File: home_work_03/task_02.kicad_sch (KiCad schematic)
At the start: 10 parts

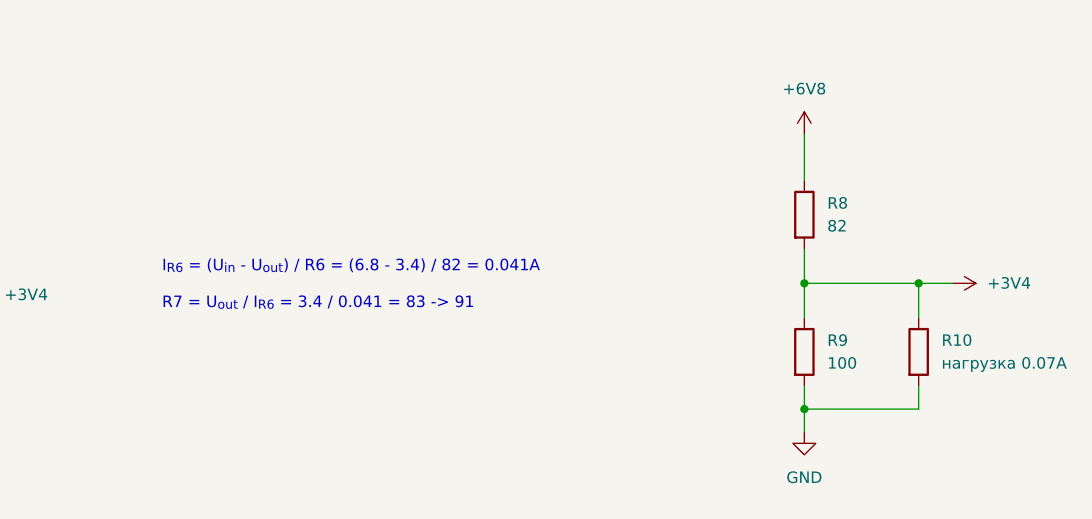
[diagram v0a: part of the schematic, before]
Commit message: fix home work 3
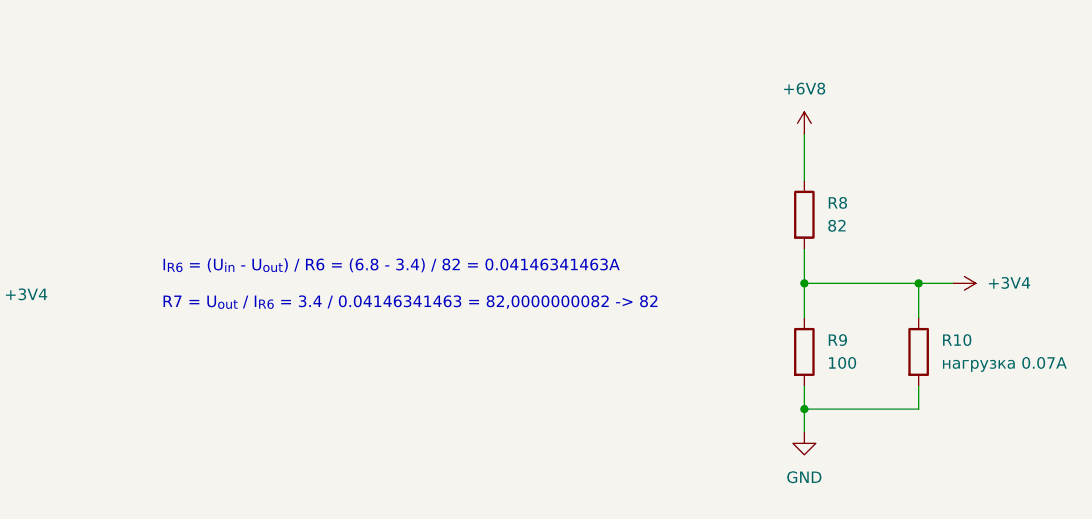
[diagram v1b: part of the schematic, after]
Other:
- note added: "I_{R6} = (U_{in} - U_{out}) / R6 = (6.8 - 3.4) / 82 = 0.04146341463A R7 = U_{out} / I_{R6} = 3.4 / 0.04146341463 = 82,0000000082 -> 82"
- note removed: "I_{R6} = (U_{in} - U_{out}) / R6 = (6.8 - 3.4) / 82 = 0.041A R7 = U_{out} / I_{R6} = 3.4 / 0.041 = 83 -> 91"
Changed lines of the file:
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@@
 		)
 	)
-	(text "I_{R6} = (U_{in} - U_{out}) / R6 = (6.8 - 3.4) / 82 = 0.041A\n\nR7 = U_{out} / I_{R6} = 3.4 / 0.041 = 83 -> 91"
+	(text "I_{R6} = (U_{in} - U_{out}) / R6 = (6.8 - 3.4) / 82 = 0.04146341463A\n\nR7 = U_{out} / I_{R6} = 3.4 / 0.04146341463 = 82,0000000082 -> 82"
 		(exclude_from_sim no)
 		(at 75.946 127 0)

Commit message: fix home work 03
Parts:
- R7: value 91 -> 82
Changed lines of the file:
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@@
 			)
 		)
-		(property "Value" "91"
+		(property "Value" "82"
 			(at 40.64 139.6999 0)
 			(effects

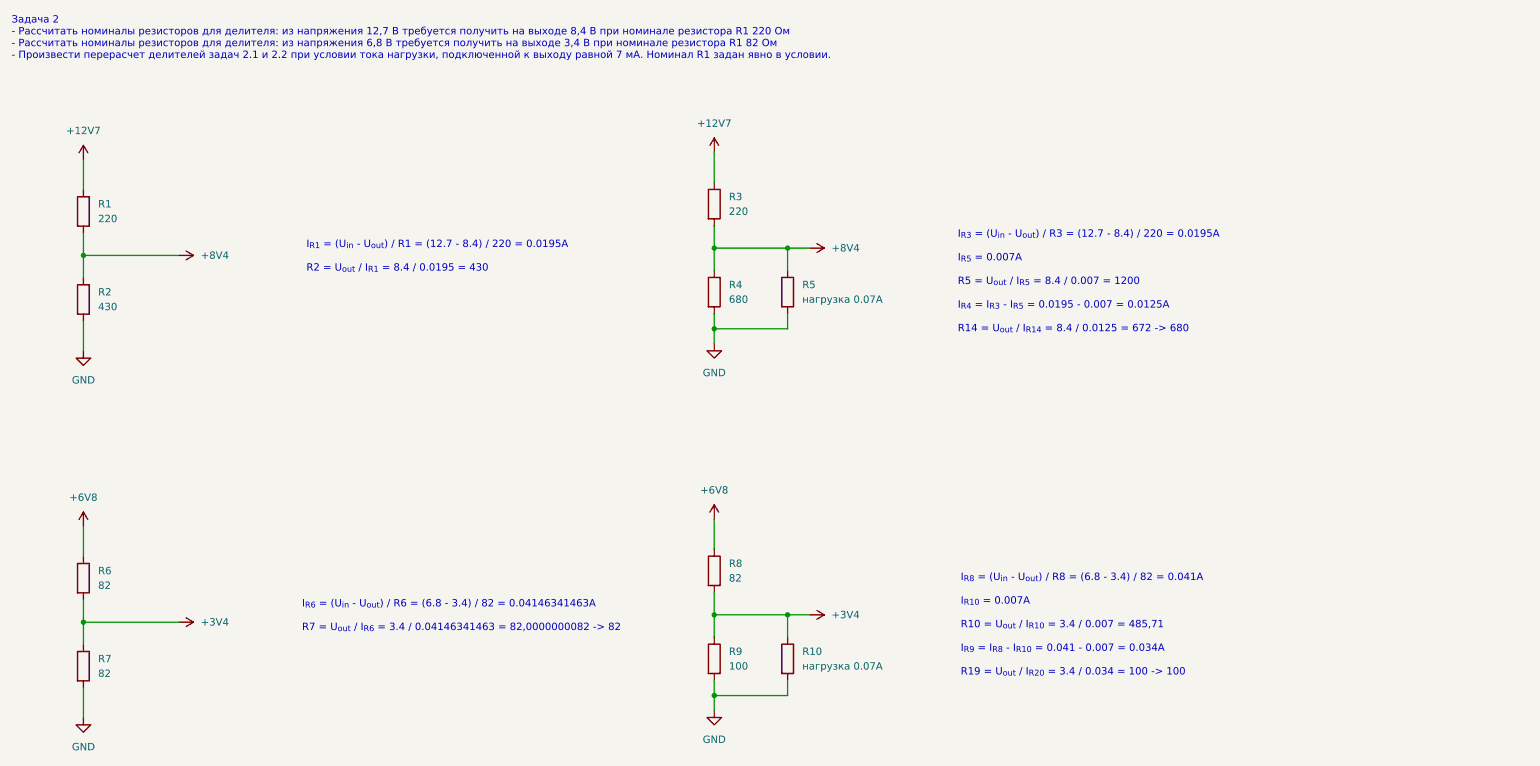
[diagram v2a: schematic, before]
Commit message: fix home work 3
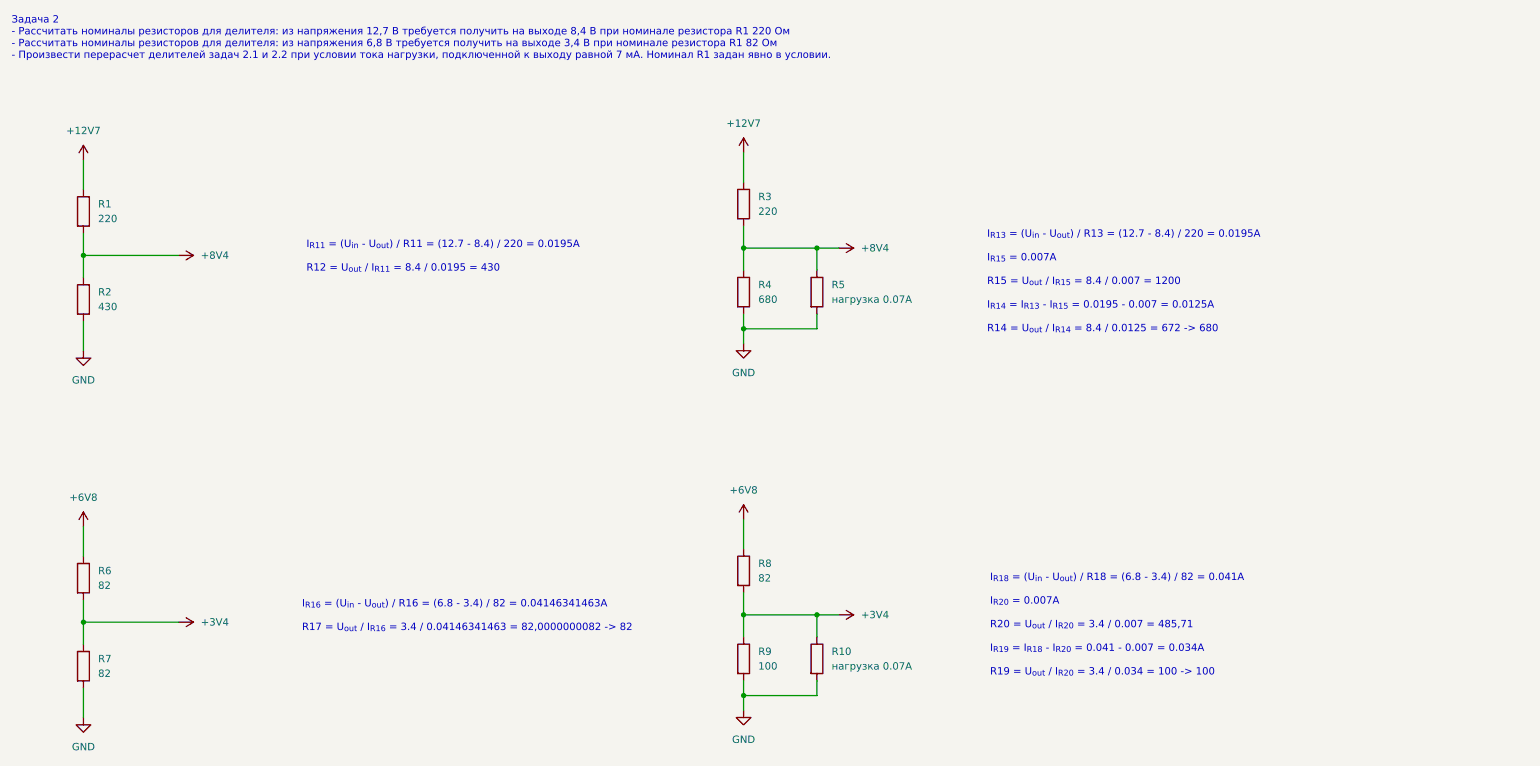
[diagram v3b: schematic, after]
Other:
- note added: "I_{R11} = (U_{in} - U_{out}) / R11 = (12.7 - 8.4) / 220 = 0.0195A R12 = U_{out} / I_{R11} = 8.4 / 0.0195 = 430"
- note added: "I_{R13} = (U_{in} - U_{out}) / R13 = (12.7 - 8.4) / 220 = 0.0195A I_{R15} = 0.007A R15 = U_{out} / I_{R15} = 8.4 / 0.007 = 1200 I_{R14} = I_{R13} - I_{R15} = 0.0195 - 0.007 = 0.0125A R14 = U_{out} / I_{R14} = 8.4 / 0.0125 = 672 -> 680"
- note added: "I_{R16} = (U_{in} - U_{out}) / R16 = (6.8 - 3.4) / 82 = 0.04146341463A R17 = U_{out} / I_{R16} = 3.4 / 0.04146341463 = 82,0000000082 -> 82"
- note added: "I_{R18} = (U_{in} - U_{out}) / R18 = (6.8 - 3.4) / 82 = 0.041A I_{R20} = 0.007A R20 = U_{out} / I_{R20} = 3.4 / 0.007 = 485,71 I_{R19} = I_{R18} - I_{R20} = 0.041 - 0.007 = 0.034A R19 = U_{out} / I_{R20} = 3.4 / 0.034 = 100 -> 100"
- note removed: "I_{R1} = (U_{in} - U_{out}) / R1 = (12.7 - 8.4) / 220 = 0.0195A R2 = U_{out} / I_{R1} = 8.4 / 0.0195 = 430"
- note removed: "I_{R3} = (U_{in} - U_{out}) / R3 = (12.7 - 8.4) / 220 = 0.0195A I_{R5} = 0.007A R5 = U_{out} / I_{R5} = 8.4 / 0.007 = 1200 I_{R4} = I_{R3} - I_{R5} = 0.0195 - 0.007 = 0.0125A R14 = U_{out} / I_{R14} = 8.4 / 0.0125 = 672 -> 680"
- note removed: "I_{R6} = (U_{in} - U_{out}) / R6 = (6.8 - 3.4) / 82 = 0.04146341463A R7 = U_{out} / I_{R6} = 3.4 / 0.04146341463 = 82,0000000082 -> 82"
- note removed: "I_{R8} = (U_{in} - U_{out}) / R8 = (6.8 - 3.4) / 82 = 0.041A I_{R10} = 0.007A R10 = U_{out} / I_{R10} = 3.4 / 0.007 = 485,71 I_{R9} = I_{R8} - I_{R10} = 0.041 - 0.007 = 0.034A R19 = U_{out} / I_{R20} = 3.4 / 0.034 = 100 -> 100"
- moved on the sheet: R10, R3, R4, R5, R8, R9
